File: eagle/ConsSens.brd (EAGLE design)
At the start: 100 x 80 mm, 6 parts

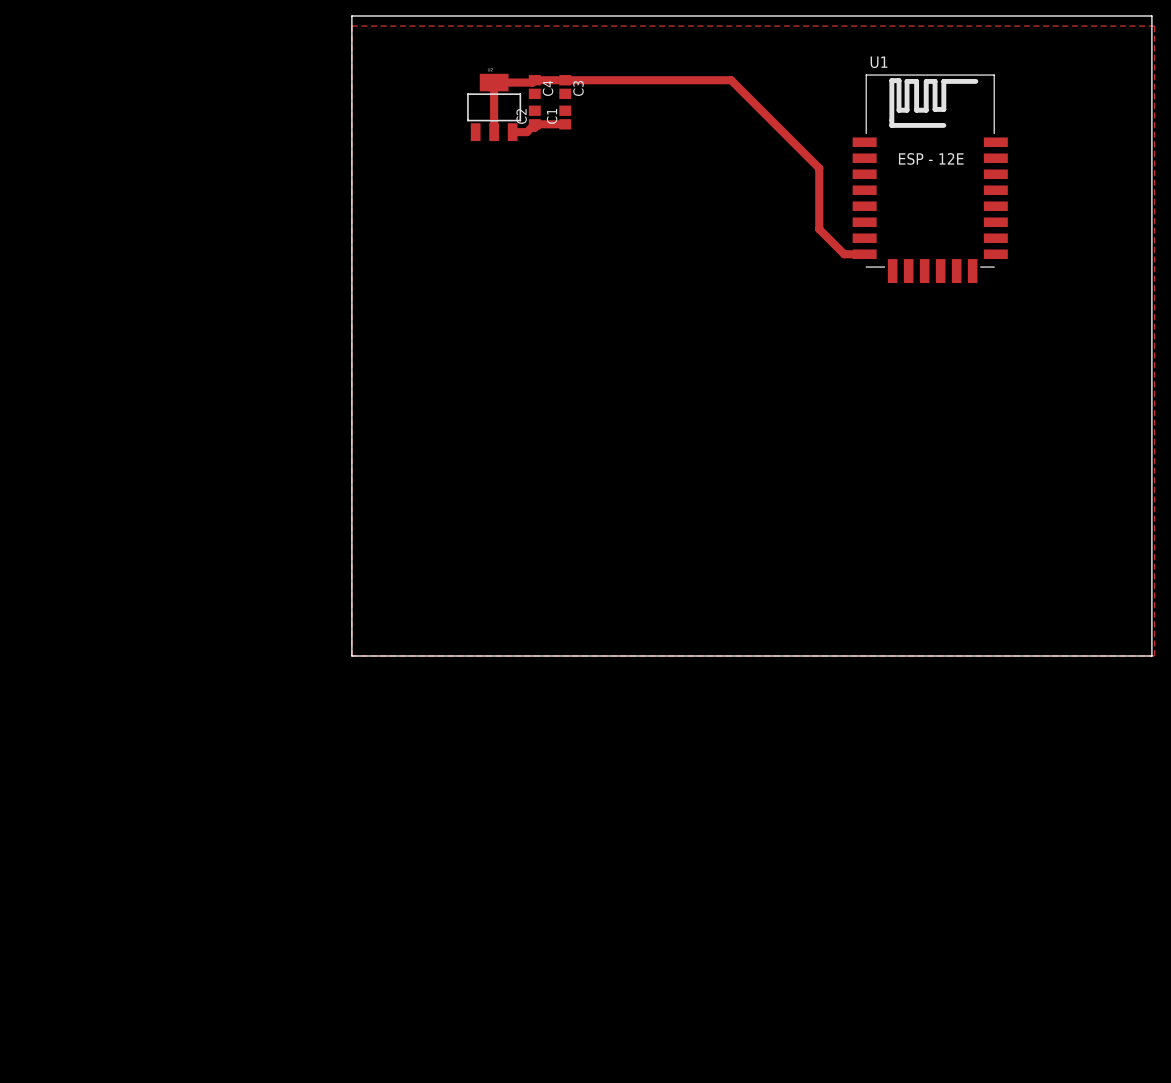
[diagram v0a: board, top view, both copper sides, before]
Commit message: some new parts added to the layout, usb-serial eagle lib added
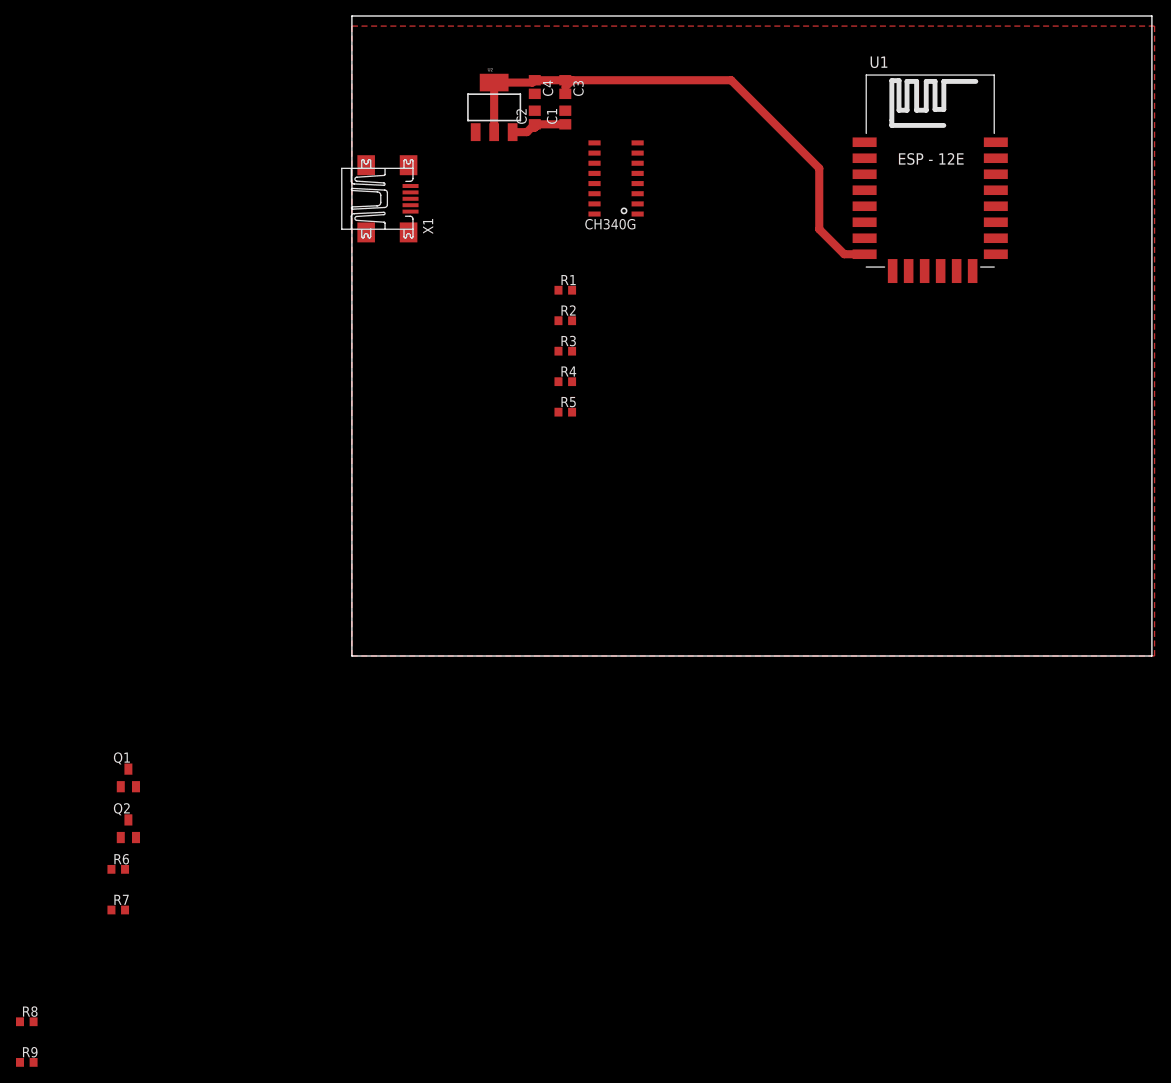
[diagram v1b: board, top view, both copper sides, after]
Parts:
- added Q1, Q2: (no value), semicon-smd-ipc:SOT23
- added R1, R2, R3, R4, R5, R6, R7: 12k, eagle-ltspice:R0603
- added R8, R9: 470, eagle-ltspice:R0603
- added U$1: CH340G, ch340g:SOIC16
- added X1: MINI-USB-SHIELD-UX60A-MB-5ST, con-hirose:UX60A-MB-5ST
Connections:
- new net +3V3: C3.1, C4.1, R1.1, R2.1, R3.1, R4.1, U$1.4, U1.VCC, U2.2, U2.4
- new net 5V: U$1.16, X1.1
- new net EN: R3.2
- new net N$1: Q1.1, R7.1
- new net N$15: U$1.3
- new net N$16: U$1.2
- new net N$2: Q2.1, R6.1
- new net N$3: Q2.2, R7.2, U$1.14
- new net N$4: Q1.2, R6.2, U$1.13
- new net N$5: U$1.6, X1.2
- new net N$6: U$1.5, X1.3
- new net N$7: R8.2
- net 3V3: no longer C3.1, C4.1, U1.VCC, U2.2, U2.4
- net GND: now also R5.1, U$1.1, X1.5
- net GPIO0: now also Q1.3, R1.2
- net GPIO15: now also R5.2
- net GPIO2: now also R2.2
- net RST: now also Q2.3, R4.2
- net RX: now also R9.1
- net TX: now also R8.1
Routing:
- net +3V3: track 0.00 -> 66.5 mm
- net 3V3: track 66.1 -> 0.00 mm

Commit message: more layout added, also new eagle libs, and datasheets
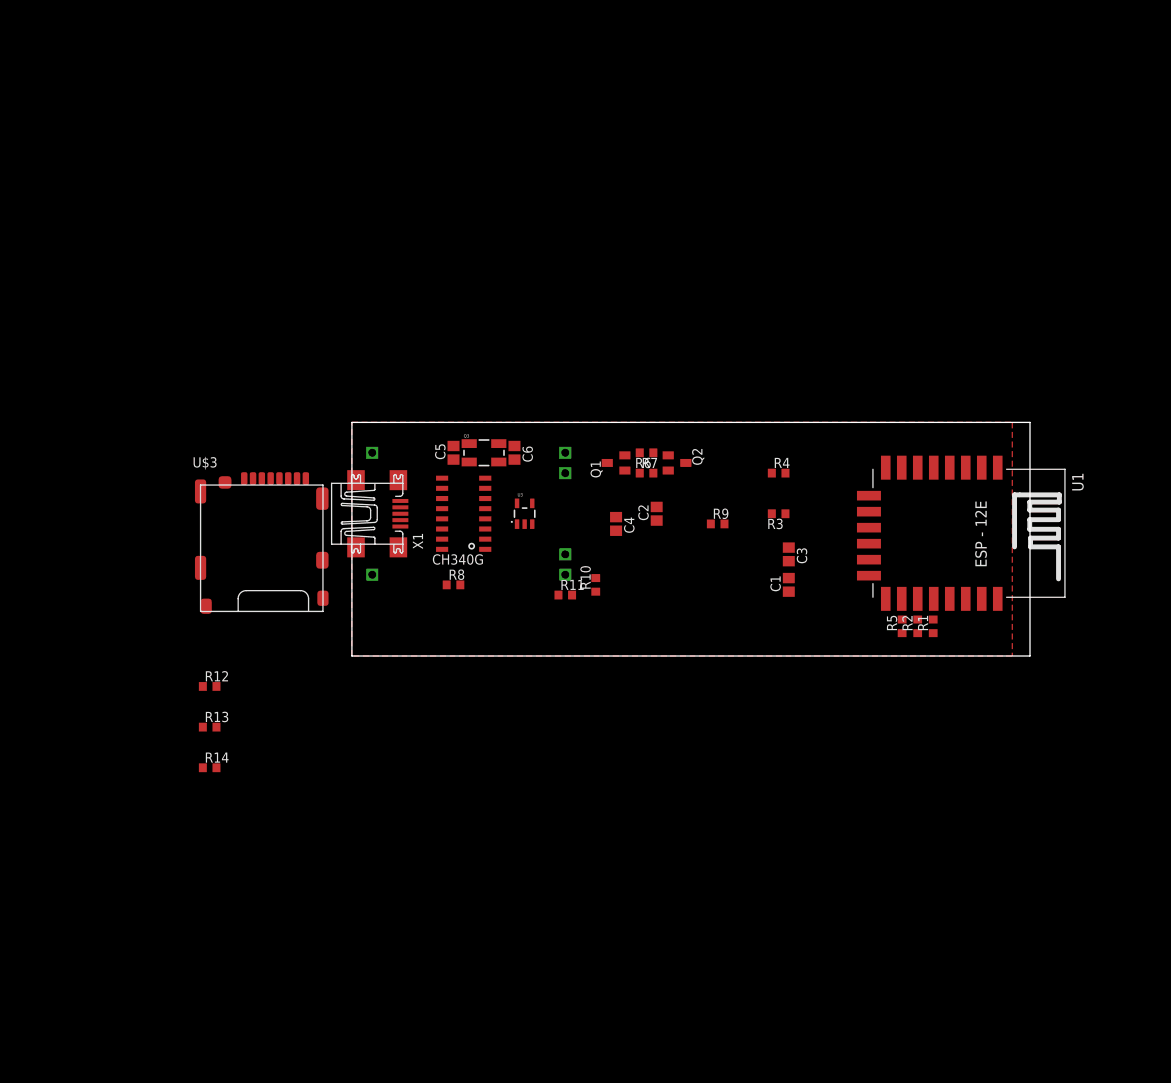
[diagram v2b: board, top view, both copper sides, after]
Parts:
- removed U2: (no value), SparkFun-PowerIC:SOT223
- added C5: 22pF, resistor:C0805
- added C6: 22pf, resistor:C0805
- added Q3: 12MHz, SparkFun-FreqCtrl:CRYSTAL-SMD-5X3
- added R10: 220k, eagle-ltspice:R0603
- added R11: 100k, eagle-ltspice:R0603
- added R12, R13, R14: 12k, eagle-ltspice:R0603
- added U$2: LIPOCHARGER, aliexpress:LIPOCHARGER
- added U$3: MICROSD_SPI_MODE, con-molex-microsd:MICRO_SD_CONNECTOR
- added U3: 3.3V, SparkFun-PowerIC:SOT23-5
- moved R9 109.5 mm to (45.7, 16.5)
- moved R7 85.7 mm to (36.8, 22.9)
- moved R6 84.1 mm to (36.8, 25.4), turned to 180 degrees
- moved Q2 82.4 mm to (40.6, 24.1), turned to 270 degrees
- moved R8 76.3 mm to (12.7, 8.89)
- moved Q1 72.6 mm to (33.0, 24.1), turned to 90 degrees
- moved C1 64.8 mm to (54.6, 8.89)
- moved C3 64.8 mm to (54.6, 12.7)
- moved R1 62.3 mm to (72.7, 3.71), turned to 90 degrees
- moved R2 58.3 mm to (70.7, 3.71), turned to 90 degrees
- moved C4 55.5 mm to (33.0, 16.5)
- moved C2 51.8 mm to (38.1, 17.8)
- moved R5 49.9 mm to (68.8, 3.71), turned to 90 degrees
- moved U$1 46.0 mm to (14.0, 17.8)
- moved U1 43.3 mm to (74.9, 15.2), turned to 270 degrees
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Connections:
- net N$16 renamed RXD0
- removed net 3V3: U1.CH_PD
- removed net 5V: U$1.16, X1.1
- removed net N$15: U$1.3
- removed net N$7: R8.2
- removed net VIN: C1.1, C2.1, U2.3
- new net N$20: U$3.8
- new net N$8: U$3.1
- new net OUT+: C1.1, C2.1, R10.2, U$2.B+, U$2.OUT+, U3.1
- new net TXD0: R8.2, U$1.3
- new net USB5V: U$1.16, U$2.IN+, X1.1
- new net XI: C6.1, Q3.3, U$1.7
- new net XO: C5.1, Q3.1, U$1.8
- net +3V3: now also U3.5; no longer U2.2, U2.4
- net ADC: now also R10.1, R11.2
- net EN: now also U1.CH_PD
- net GND: now also C5.2, C6.2, R11.1, R12.2, R13.2, R14.2, U$2.IN-, U$2.OUT-, U$3.4, U$3.6, U3.2; no longer U2.1
- net GPIO12: now also R14.1, U$3.7
- net GPIO13: now also R12.1, U$3.3
- net GPIO14: now also U$3.5
- net GPIO15: now also R13.1, U$3.2
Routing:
- net +3V3: track 66.5 -> 0.00 mm
- net VIN: track 7.58 -> 0.00 mm
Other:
- board size 100 x 80 mm -> 84.8 x 29.2 mm

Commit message: first routing
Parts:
- added 1-WIRE: (no value), con-lstb:MA03-1
- added I2C: (no value), con-lstb:MA04-1
- moved R14 75.8 mm to (49.5, 21.0), flipped to the bottom
- moved U$3 73.7 mm to (62.2, 15.2), flipped to the bottom, turned to 270 degrees
- moved R13 72.9 mm to (49.5, 19.1), flipped to the bottom
- moved R12 70.5 mm to (49.5, 17.1), flipped to the bottom
- moved C1 49.9 mm to (5.08, 3.17), turned to 270 degrees
- moved C3 40.5 mm to (15.2, 3.17)
- moved C2 33.2 mm to (8.26, 3.17), turned to 270 degrees
- moved R9 27.7 mm to (18.4, 12.1), turned to 180 degrees
- moved C4 20.7 mm to (17.1, 3.17)
- moved U3 17.4 mm to (12.1, 3.17), turned to 270 degrees
- moved R4 16.1 mm to (69.2, 25.4), turned to 270 degrees
- moved R3 14.3 mm to (65.4, 25.4), turned to 270 degrees
- moved U1 11.5 mm to (63.5, 14.0)
- moved R1 11.5 mm to (61.2, 2.44)
- moved R2 11.5 mm to (59.3, 2.44)
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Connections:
- new net GPO4: I2C.2
- net +3V3: now also 1-WIRE.1, I2C.1
- net GND: now also 1-WIRE.3, I2C.4
- net GPIO14: now also 1-WIRE.2
- net GPIO5: now also I2C.3
- net OUT+: now also U3.3
- net RXD0: now also R9.2
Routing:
- net GND: track 0.00 -> 148.8 mm, vias 0 -> 5
- net +3V3: track 0.00 -> 124.0 mm, vias 0 -> 2
- net ADC: track 0.00 -> 62.8 mm
- net TX: track 0.00 -> 61.2 mm, vias 0 -> 2
- net RX: track 0.00 -> 58.7 mm, vias 0 -> 2
- net GPIO0: track 0.00 -> 55.5 mm, vias 0 -> 2
- net GPIO5: track 0.00 -> 37.7 mm, vias 0 -> 2
- net RST: track 0.00 -> 36.0 mm
- net N$4: track 0.00 -> 34.7 mm, vias 0 -> 2
- net GPIO15: track 0.00 -> 34.1 mm, vias 0 -> 3
- net N$3: track 0.00 -> 33.3 mm, vias 0 -> 2
- net GPIO12: track 0.00 -> 33.0 mm, vias 0 -> 2
- net OUT+: track 0.00 -> 30.2 mm
- net GPIO14: track 0.00 -> 25.1 mm, vias 0 -> 1
- net USB5V: track 0.00 -> 23.4 mm, vias 0 -> 1
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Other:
- board size 84.8 x 29.2 mm -> 77.1 x 27.9 mm

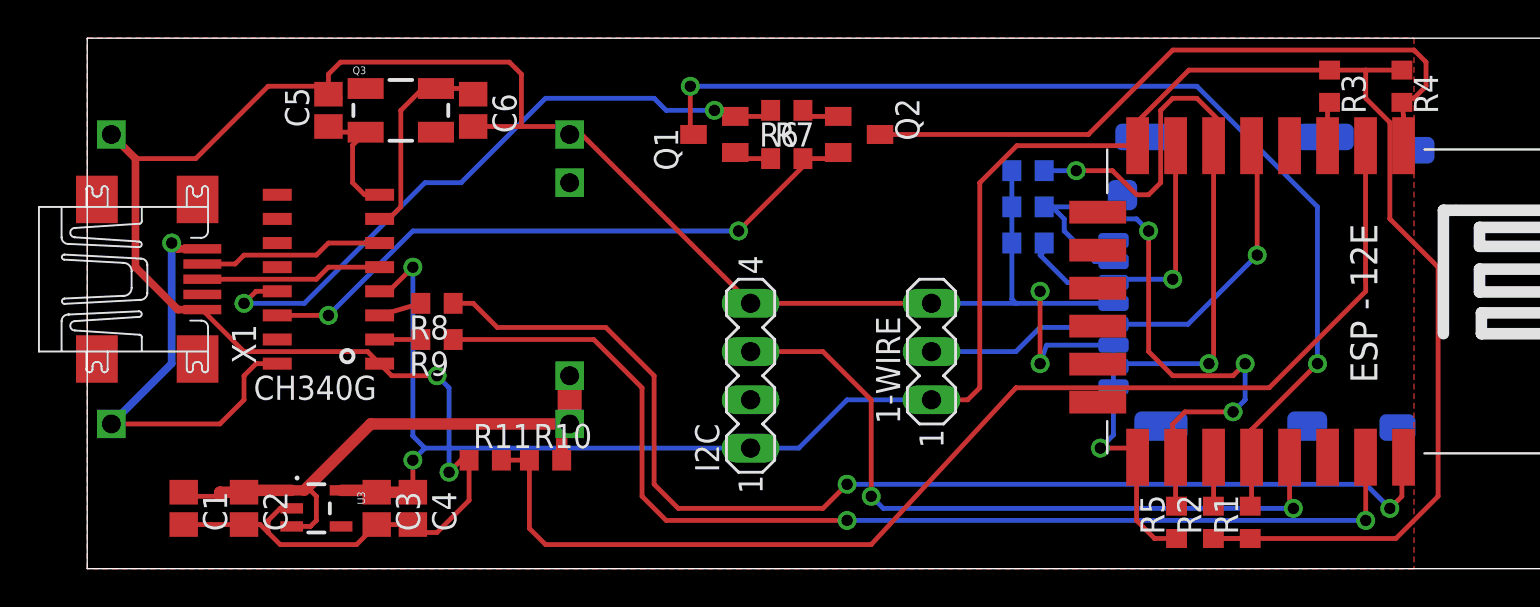
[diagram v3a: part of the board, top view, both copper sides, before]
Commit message: Fixed some design errors in board layout
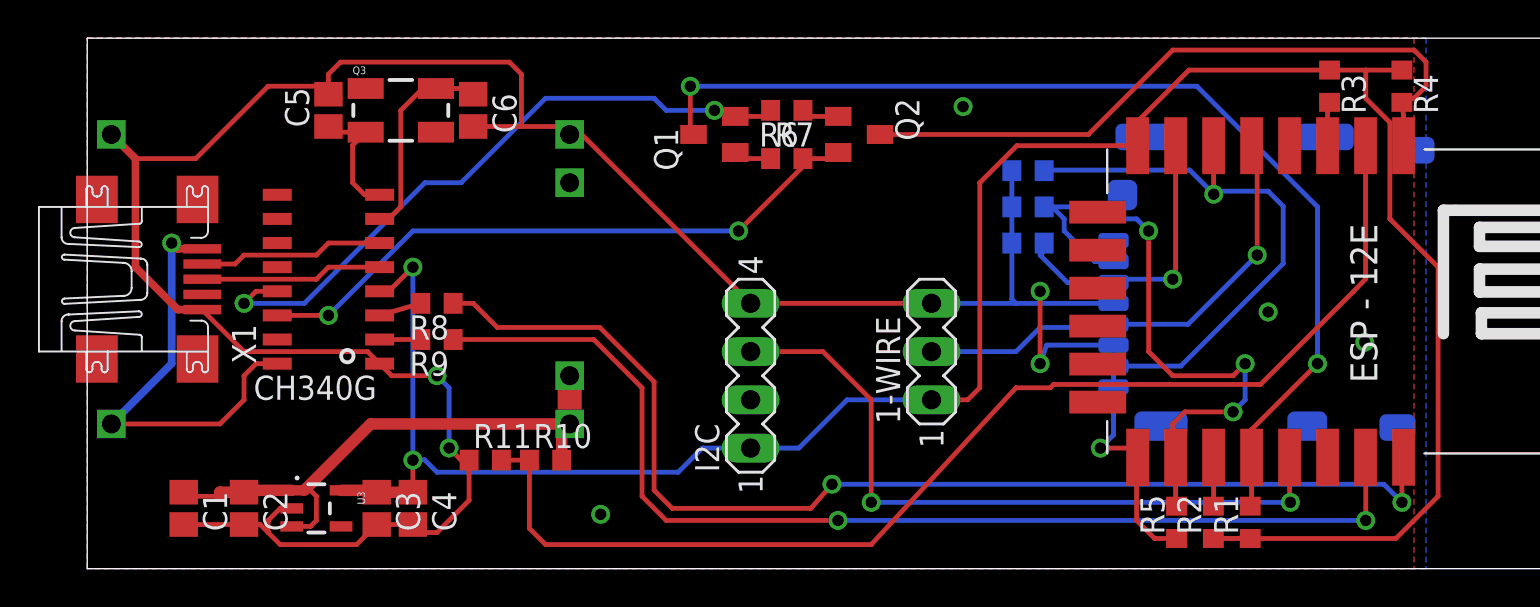
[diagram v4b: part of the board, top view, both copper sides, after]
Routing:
- net GPIO12: track 33.0 -> 30.7 mm, vias 2 -> 1
- net GND: track 148.8 -> 147.6 mm, vias 5 -> 9
- net +3V3: track 124.0 -> 125.0 mm
- added copper zone on layer 16, net GND

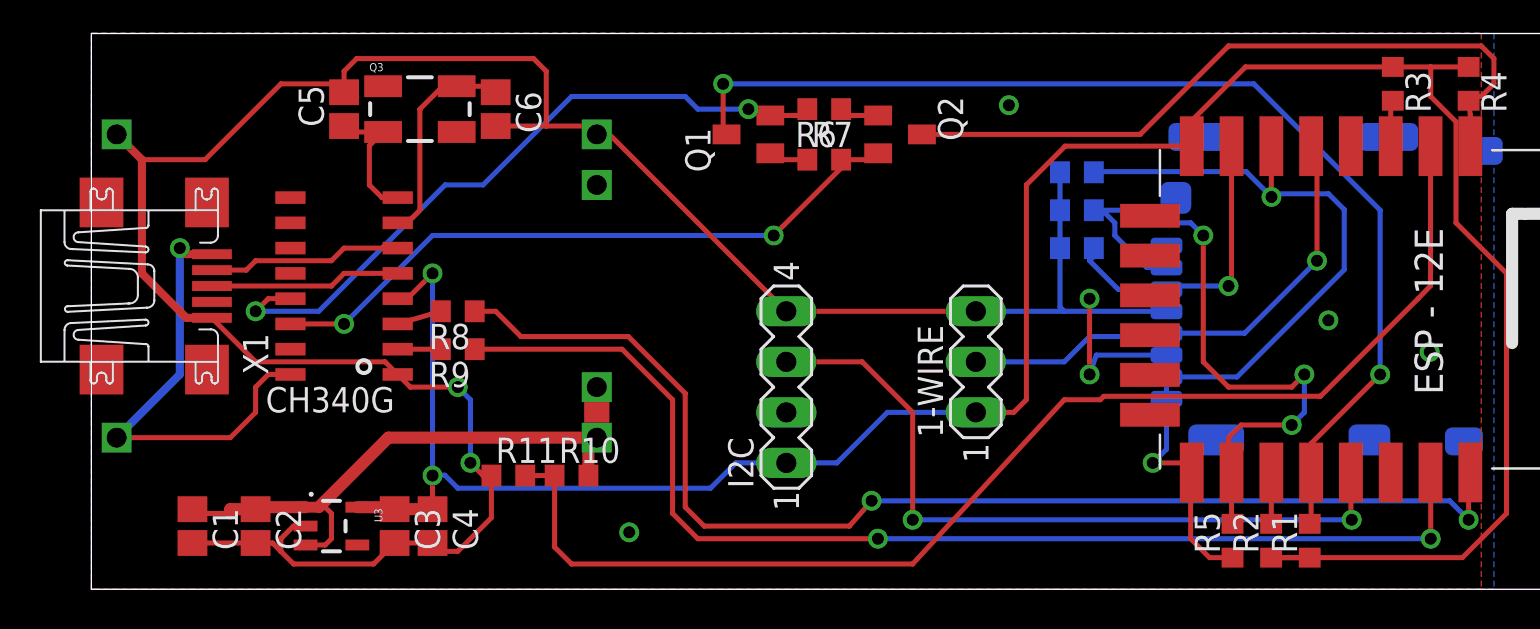
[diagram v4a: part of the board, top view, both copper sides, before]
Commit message: fixed wrong size from LiPo Charge Modul
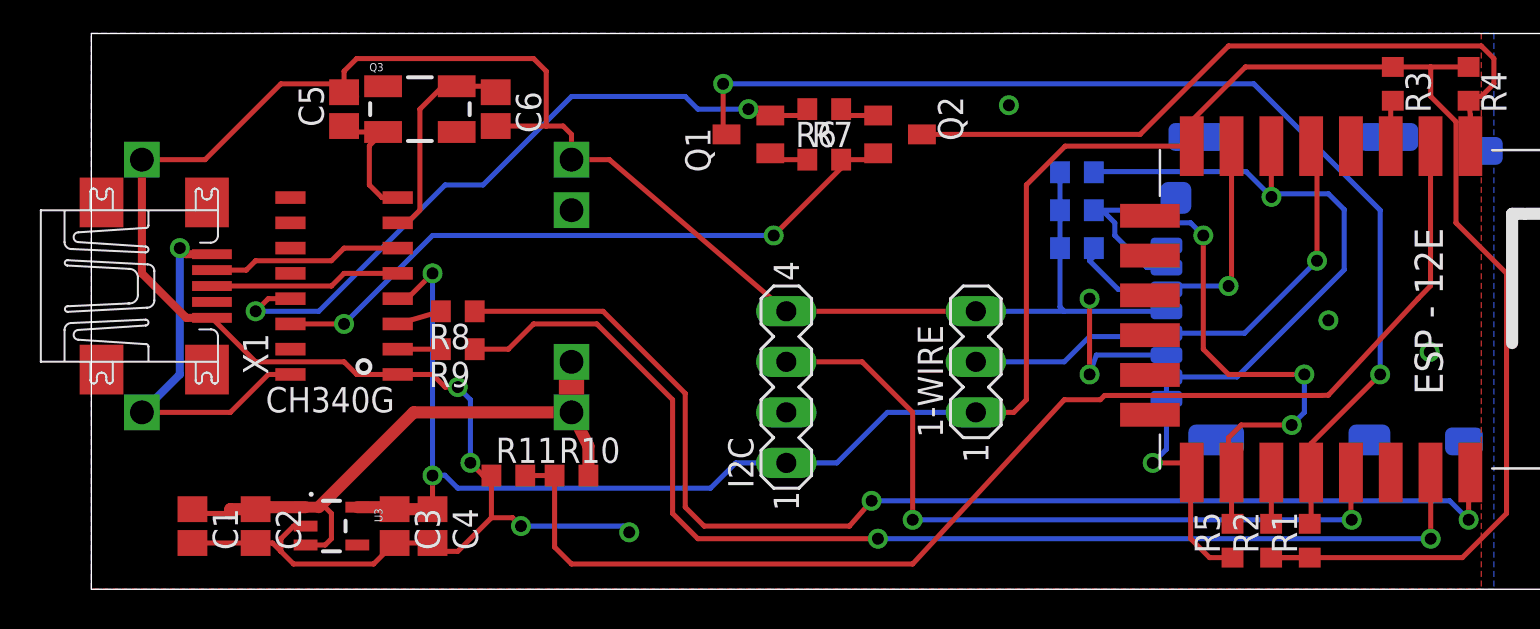
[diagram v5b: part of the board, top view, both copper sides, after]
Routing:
- net GND: track 147.6 -> 153.4 mm, vias 9 -> 10
- net USB5V: track 23.4 -> 19.0 mm
- net RX: track 58.7 -> 59.7 mm
- net GPIO15: track 34.1 -> 33.2 mm
- net OUT+: track 30.2 -> 30.7 mm
